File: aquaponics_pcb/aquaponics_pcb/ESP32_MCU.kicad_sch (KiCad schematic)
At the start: 2 parts, among them IC1 ESP32-S3-WROOM-1U-N8, J2 2338792-1

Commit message: update ESP32 MCU sch, add LDO and pinouts
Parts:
- added C1, C4: 10uF, Capacitor_SMD:C_0603_1608Metric_Pad1.08x0.95mm_HandSolder, symbol Device:C
- added C2, C5, C7, C8: 1uF, Capacitor_SMD:C_0603_1608Metric_Pad1.08x0.95mm_HandSolder, symbol Device:C
- added C3, C6: 100nF, Capacitor_SMD:C_0603_1608Metric_Pad1.08x0.95mm_HandSolder, symbol Device:C
- added IC2: AZ1117CH-3.3TRG1, SOT230P700X180-4N, symbol SamacSys_Parts:AZ1117CH-3.3TRG1
- added S1, S2: TS04-66-50-BK-260-SMT-TR, TS046650BK260SMTTR, symbol SamacSys_Parts:TS04-66-50-BK-260-SMT-TR
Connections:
- net +5V_USB: now also C4.1, C5.1, C6.1, IC2.3 (INPUT)
- net GND: now also IC1.1 (GND_1), IC1.40 (GND_2), IC1.41 (GND_3), IC1.42 (GND_4), IC1.43 (GND_5), IC1.44 (GND_6), IC1.45 (GND_7), IC1.46 (GND_8), IC1.47 (GND_9), IC1.48 (GND_10), IC1.49 (GND_11), C1.2, C2.2, C3.2, C4.2, C5.2, C6.2, C7.1, C8.1, IC2.1 (ADJ/GND), S1.2 (COM_1), S2.2 (COM_1)
- net UART_1_MCU_TX: now reaches IC1.10 (RTC_GPIO17/GPIO17/U1TXD/ADC2_CH6)
- net UART_1_MCU_RX: now reaches IC1.11 (RTC_GPIO18/GPIO18/U1RXD/ADC2_CH7/CLK_OUT3)
- net +3V3: now reaches IC1.2 (3V3)
- net +3V3: now also C1.1, C2.1, C3.1, IC2.4 (VOUT)
- net UART_2_MCU_TX: now reaches IC1.25 (SPICLK_N_DIFF/GPIO48/SUBSPICLK_N_DIFF)
- net UART_2_MCU_RX: now reaches IC1.26 (GPIO45)
- net GPIO0: now reaches IC1.27 (RTC_GPIO0/GPIO0)
- net GPIO0: now also C7.2, S1.1 (NO_1)
- net EN: now reaches IC1.3 (EN)
- net EN: now also C8.2, S2.1 (NO_1)
- net UART_0_MCU_RX: now reaches IC1.36 (U0RXD/GPIO44/CLK_OUT2)
- net UART_0_MCU_TX: now reaches IC1.37 (U0TXD/GPIO43/CLK_OUT1)
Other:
- moved on the sheet: IC1

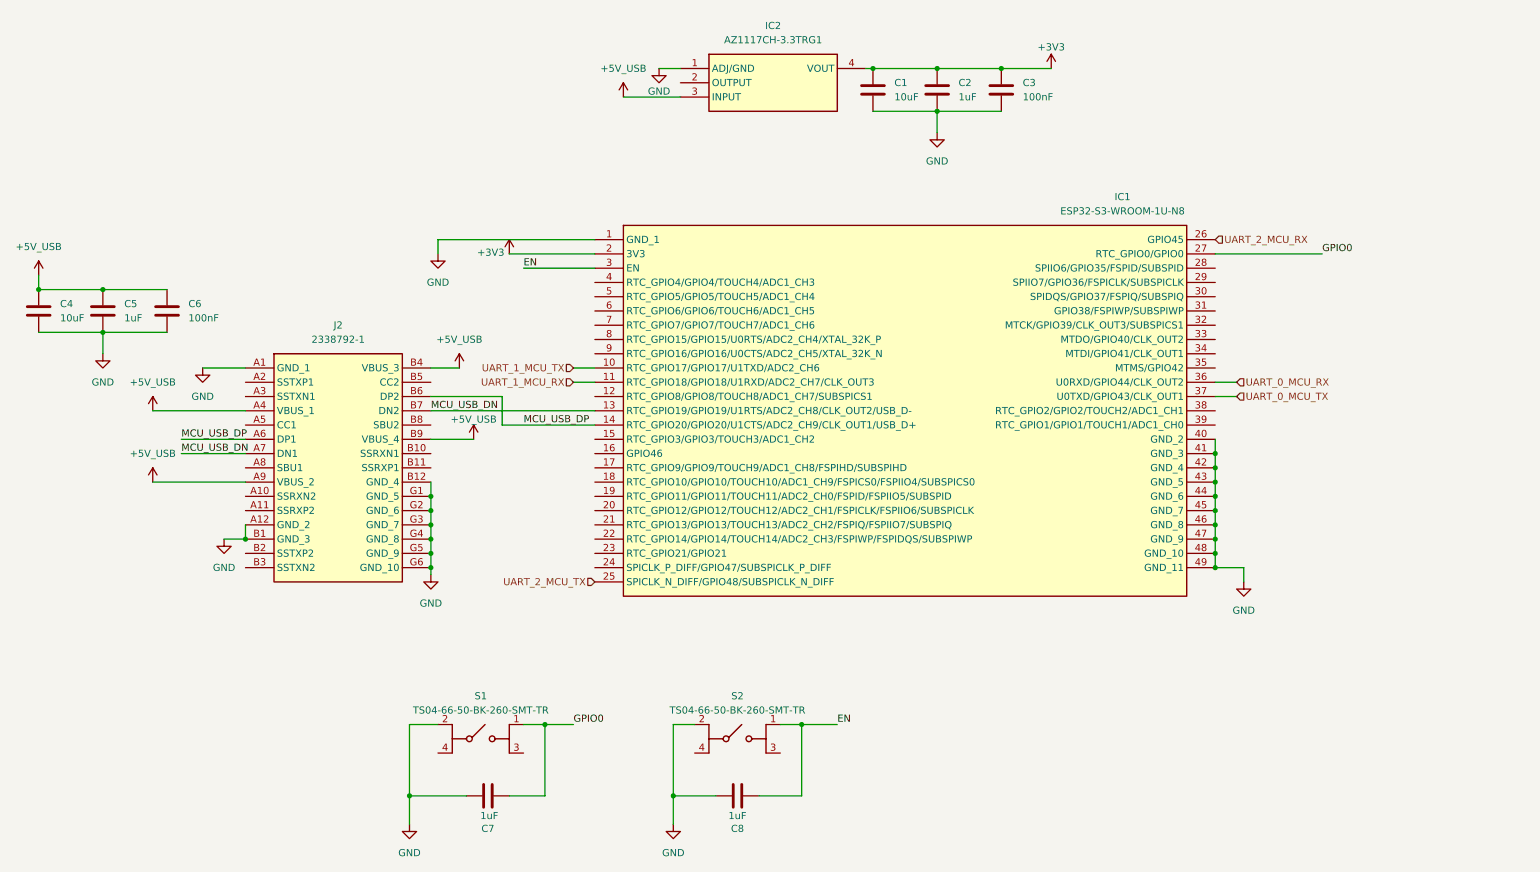
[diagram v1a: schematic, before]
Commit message: finish MCU and start logic isolation block
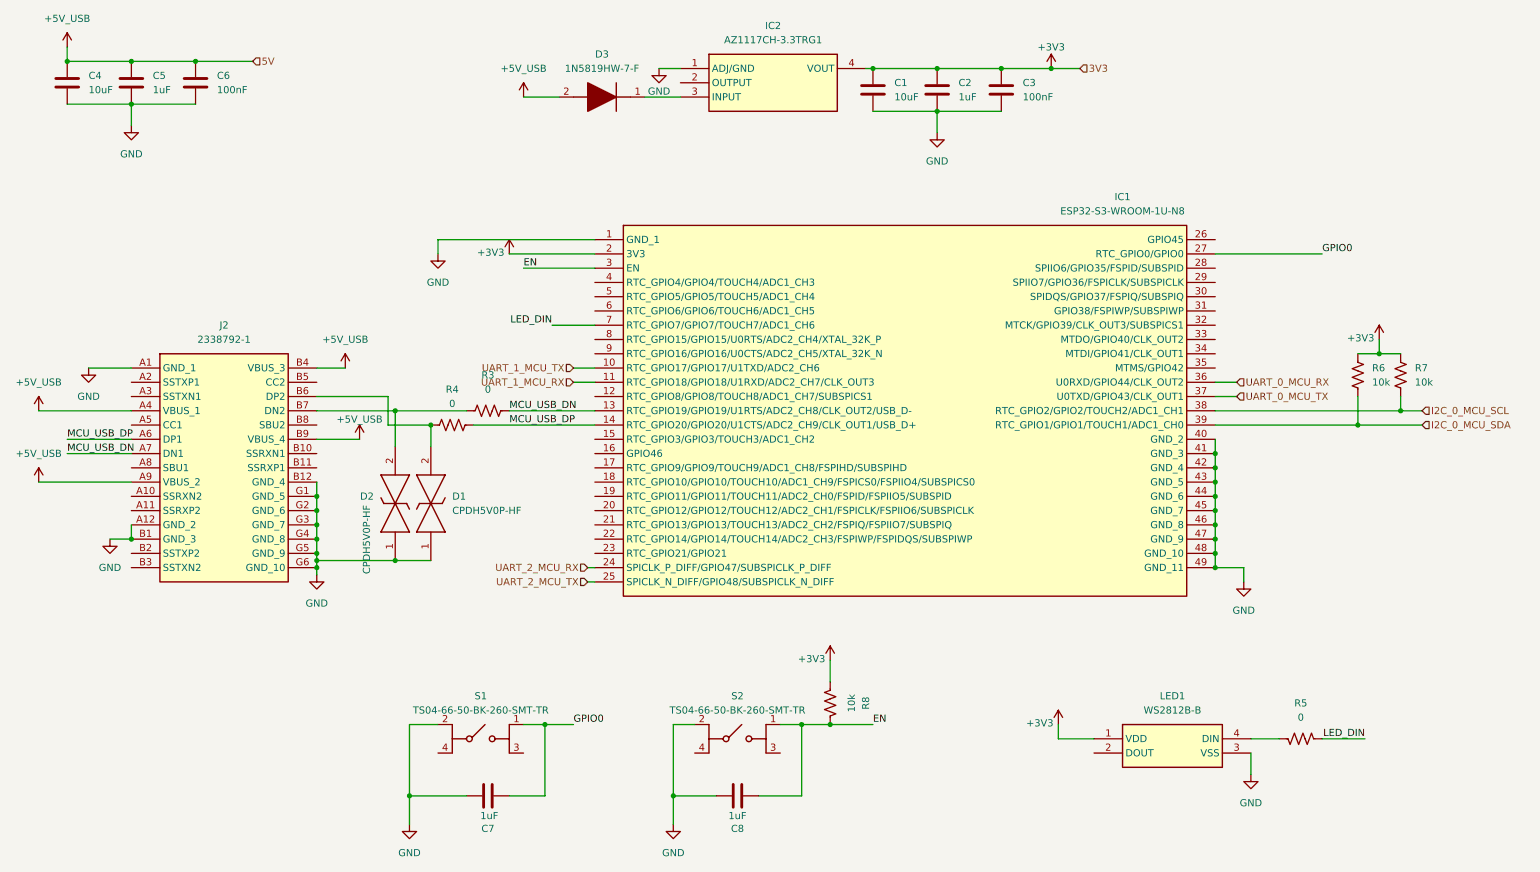
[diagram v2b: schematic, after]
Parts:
- added D1, D2: CPDH5V0P-HF, SamacSys_Parts:CPDH5V0PHF, symbol SamacSys_Parts:CPDH5V0P-HF
- added D3: 1N5819HW-7-F, SamacSys_Parts:SOD3716X145N, symbol SamacSys_Parts:1N5819HW-7-F
- added LED1: WS2812B-B, SamacSys_Parts:WS2812BB, symbol SamacSys_Parts:WS2812B-B
- added R3, R4, R5: 0, Resistor_SMD:R_0603_1608Metric_Pad0.98x0.95mm_HandSolder, symbol Device:R_US
- added R6, R7, R8: 10k, Resistor_SMD:R_0603_1608Metric_Pad0.98x0.95mm_HandSolder, symbol Device:R_US
- IC1: footprint ESP32S3WROOM1UN8 -> SamacSys_Parts:ESP32S3WROOM1UN8
- IC2: footprint SOT230P700X180-4N -> SamacSys_Parts:SOT230P700X180-4N
- J2: footprint 23387921 -> SamacSys_Parts:23387921
- S1, S2: footprint TS046650BK260SMTTR -> SamacSys_Parts:TS046650BK260SMTTR
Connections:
- net +3V3: now also LED1.1 (VDD), R6.2, R7.2, R8.2
- net +5V_USB: now also D3.2 (A); no longer IC2.3 (INPUT)
- net EN: now also R8.1
- net GND: now also D1.1, D2.1, LED1.3 (VSS)
- net MCU_USB_DN: now also R3.2; no longer J2.B7 (DN2)
- net MCU_USB_DP: now also R4.2; no longer J2.B6 (DP2)
- net UART_2_MCU_RX: now also IC1.24 (SPICLK_P_DIFF/GPIO47/SUBSPICLK_P_DIFF); no longer IC1.26 (GPIO45)
- net I2C_0_MCU_SCL: now reaches IC1.38 (RTC_GPIO2/GPIO2/TOUCH2/ADC1_CH1)
- net I2C_0_MCU_SCL: now also R7.1
- net I2C_0_MCU_SDA: now reaches IC1.39 (RTC_GPIO1/GPIO1/TOUCH1/ADC1_CH0)
- net I2C_0_MCU_SDA: now also R6.1
- net LED_DIN: now reaches IC1.7 (RTC_GPIO7/GPIO7/TOUCH7/ADC1_CH6)
- net LED_DIN: now also R5.1
- new net: D1.2, J2.B6 (DP2), R4.1
- new net: D2.2, J2.B7 (DN2), R3.1
- new net: D3.1 (K), IC2.3 (INPUT)
- new net: LED1.4 (DIN), R5.2
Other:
- moved on the sheet: C4, C5, C6, J2

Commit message: add ezo datasheets, update motor schematic and add 2 motors
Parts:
- renumbered C4 to C1, C5 to C2, C6 to C3, C7 to C4, C8 to C5, C1 to C6, C2 to C7, C3 to C8, D2 to D1, D1 to D2, IC2 to IC1, IC1 to IC2, R5 to R10, R6 to R11, R7 to R12, R4 to R7, R3 to R8, R8 to R9
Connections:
- net M_NSLEEP: now reaches IC2.12 (RTC_GPIO8/GPIO8/TOUCH8/ADC1_CH7/SUBSPICS1)
- net M2_IPROPI: now reaches IC2.17 (RTC_GPIO9/GPIO9/TOUCH9/ADC1_CH8/FSPIHD/SUBSPIHD)
- net M_NFAULT: now reaches IC2.23 (RTC_GPIO21/GPIO21)
- net ISO_EN: now reaches IC2.35 (MTMS/GPIO42)
- net M_PWM1: now reaches IC2.4 (RTC_GPIO4/GPIO4/TOUCH4/ADC1_CH3)
- net M_PWM2: now reaches IC2.5 (RTC_GPIO5/GPIO5/TOUCH5/ADC1_CH4)
- net M_IPROPI: now reaches IC2.6 (RTC_GPIO6/GPIO6/TOUCH6/ADC1_CH5)
- net M2_PWM1: now reaches IC2.8 (RTC_GPIO15/GPIO15/U0RTS/ADC2_CH4/XTAL_32K_P)
- net M2_PWM2: now reaches IC2.9 (RTC_GPIO16/GPIO16/U0CTS/ADC2_CH5/XTAL_32K_N)

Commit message: finish ground and power pours. fix rules and run final DRC. export gerbers
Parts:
- C1, C6: JLCPCB Part # (none) -> C194427; LCSC Part Number (none) -> C194427
- C2, C4, C5, C7: JLCPCB Part # (none) -> C15849; LCSC Part Number (none) -> C15849
- C3, C8: JLCPCB Part # (none) -> C14663; LCSC Part Number (none) -> C14663
- D1, D2: JLCPCB Part # (none) -> C2443345; LCSC Part Number (none) -> C2443345
- R10, R7, R8: JLCPCB Part # (none) -> C2906974; LCSC Part Number (none) -> C2906974
- R11, R12, R9: JLCPCB Part # (none) -> C98220; LCSC Part Number (none) -> C98220
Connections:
- net MCU_USB_DN: now also D1.2, J2.B7 (DN2), R8.1; no longer IC2.13 (RTC_GPIO19/GPIO19/U1RTS/ADC2_CH8/CLK_OUT2/USB_D-), R8.2
- net MCU_USB_DP: now also D2.2, J2.B6 (DP2), R7.1; no longer IC2.14 (RTC_GPIO20/GPIO20/U1CTS/ADC2_CH9/CLK_OUT1/USB_D+), R7.2
- new net: IC2.14 (RTC_GPIO20/GPIO20/U1CTS/ADC2_CH9/CLK_OUT1/USB_D+), R7.2
- new net: IC2.13 (RTC_GPIO19/GPIO19/U1RTS/ADC2_CH8/CLK_OUT2/USB_D-), R8.2
